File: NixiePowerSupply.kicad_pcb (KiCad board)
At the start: 2 copper layers, 50.8 x 38.1 mm, 17 parts, among them J1 BARREL_JACK, P1 CONN_01X03, P2 CONN_01X02, T1 IRF644, U1 MAX1771

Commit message: More layout
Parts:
- moved C5 3.31 mm to (65.0, 48.8), turned to 0 degrees
- moved R1 2.05 mm to (73.7, 52.8)
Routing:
- net Net-(C1-Pad1): track 25.3 -> 49.5 mm
- net GND: track 14.1 -> 21.4 mm, vias 8 -> 9
- net Net-(R1-Pad1): track 0.00 -> 6.39 mm
- net Net-(R2-Pad2): track 0.00 -> 6.00 mm
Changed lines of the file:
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@@
   (general
     (links 34)
-    (no_connects 33)
+    (no_connects 17)
     (area 40.669999 24.315 97.108334 63.550001)
     (thickness 1.6)
     (drawings 4)
-    (tracks 25)
+    (tracks 47)
     (zones 0)
     (modules 17)
@@
   )
   (setup
-    (last_trace_width 0.508)
+    (last_trace_width 1.016)
     (user_trace_width 0.508)
     (user_trace_width 1.016)
@@
   )
   (module Capacitors_Tantalum_SMD:CP_Tantalum_Case-X_EIA-7343-43_Hand (layer F.Cu)
-    (at 62.23 46.99 270)
+    (at 65.024 48.768)
     (descr "Tantalum capacitor, Case X, EIA 7343-43, 7.3x4.2x4.0mm, Hand soldering footprint")
     (tags "capacitor tantalum smd")
     (attr smd)
-    (fp_text reference C5 (at 0 -3.85 270) (layer F.SilkS)
-      (effects (font (size 1 1) (thickness 0.15)))
-    )
-    (fp_text value 10uF,25V (at 0 3.85 270) (layer F.Fab)
+    (fp_text reference C5 (at 0 -3.85) (layer F.SilkS)
+      (effects (font (size 1 1) (thickness 0.15)))
+    )
+    (fp_text value 10uF,25V (at 0 3.85) (layer F.Fab)
       (effects (font (size 1 1) (thickness 0.15)))
     )
@@
     (fp_line (start -5.95 2.35) (end 3.65 2.35) (layer F.SilkS) (width 0.12))
     (fp_line (start -5.95 -2.35) (end -5.95 2.35) (layer F.SilkS) (width 0.12))
-    (pad 1 smd rect (at -3.775 0 270) (size 3.75 2.7) (layers F.Cu F.Paste F.Mask)
+    (pad 1 smd rect (at -3.775 0) (size 3.75 2.7) (layers F.Cu F.Paste F.Mask)
       (net 9 "Net-(C1-Pad1)"))
-    (pad 2 smd rect (at 3.775 0 270) (size 3.75 2.7) (layers F.Cu F.Paste F.Mask)
+    (pad 2 smd rect (at 3.775 0) (size 3.75 2.7) (layers F.Cu F.Paste F.Mask)
       (net 1 GND))
     (model Capacitors_Tantalum_SMD.3dshapes/CP_Tantalum_Case-X_EIA-7343-43.wrl
@@
   )
   (module Resistors_SMD:R_0805_HandSoldering (layer F.Cu)
-    (at 71.755 52.07 180)
+    (at 73.66 52.832 180)
     (descr "Resistor SMD 0805, hand soldering")
     (tags "resistor 0805")
@@
   (gr_line (start 95.25 25.4) (end 95.25 63.5) (layer Edge.Cuts) (width 0.1))
   (gr_line (start 44.45 25.4) (end 95.25 25.4) (layer Edge.Cuts) (width 0.1))
+  (segment (start 68.799 48.768) (end 68.799 49.321) (width 1.016) (layer F.Cu) (net 1))
+  (segment (start 68.799 49.321) (end 72.31 52.832) (width 1.016) (layer F.Cu) (net 1))
+  (segment (start 66.675 44.41) (end 65.318 44.41) (width 1.016) (layer F.Cu) (net 1))
+  (segment (start 65.318 44.41) (end 65.024 44.704) (width 1.016) (layer F.Cu) (net 1))
+  (via (at 65.024 44.704) (size 0.6) (drill 0.4) (layers F.Cu B.Cu) (net 1))
   (segment (start 91.44 34.036) (end 92.964 34.036) (width 0.508) (layer B.Cu) (net 1))
   (via (at 92.964 34.036) (size 1.016) (drill 0.508) (layers F.Cu B.Cu) (net 1))
@@
   (segment (start 63.580302 30.48) (end 71.755 30.48) (width 3.81) (layer F.Cu) (net 4))
   (segment (start 61.317651 28.217349) (end 63.580302 30.48) (width 3.81) (layer F.Cu) (net 4))
+  (segment (start 75.01 52.832) (end 77.798 52.832) (width 1.016) (layer F.Cu) (net 5))
+  (segment (start 77.798 52.832) (end 77.925 52.705) (width 1.016) (layer F.Cu) (net 5))
+  (segment (start 80.825 53.955) (end 79.175 53.955) (width 1.016) (layer F.Cu) (net 5))
+  (segment (start 79.175 53.955) (end 77.925 52.705) (width 1.016) (layer F.Cu) (net 5))
+  (segment (start 85.725 54.115) (end 83.485 54.115) (width 1.016) (layer F.Cu) (net 6))
+  (segment (start 83.485 54.115) (end 80.825 51.455) (width 1.016) (layer F.Cu) (net 6))
+  (segment (start 66.675 41.91) (end 69.055 41.91) (width 1.016) (layer F.Cu) (net 9))
+  (segment (start 61.249 48.768) (end 61.249 44.679) (width 2.032) (layer F.Cu) (net 9))
+  (segment (start 61.249 44.679) (end 64.018 41.91) (width 2.032) (layer F.Cu) (net 9))
+  (segment (start 64.018 41.91) (end 66.675 41.91) (width 2.032) (layer F.Cu) (net 9))
+  (segment (start 61.249 48.768) (end 60.724 48.768) (width 2.032) (layer F.Cu) (net 9))
+  (segment (start 60.724 48.768) (end 58.442 51.05) (width 2.032) (layer F.Cu) (net 9))
+  (segment (start 58.442 51.05) (end 54.895 51.05) (width 2.032) (layer F.Cu) (net 9))
+  (segment (start 55.682 51.05) (end 54.895 51.05) (width 1.524) (layer F.Cu) (net 9))
+  (segment (start 54.895 53.34) (end 54.895 51.05) (width 3.81) (layer F.Cu) (net 9))
+  (segment (start 54.895 55.88) (end 54.895 53.34) (width 3.81) (layer F.Cu) (net 9))
+  (segment (start 48.93 45.085) (end 48.93 50.245) (width 3.81) (layer F.Cu) (net 9))
+  (segment (start 48.93 50.245) (end 49.735 51.05) (width 3.81) (layer F.Cu) (net 9))
+  (segment (start 49.735 51.05) (end 54.895 51.05) (width 3.81) (layer F.Cu) (net 9))
   (segment (start 54.895 55.88) (end 60.325 55.88) (width 2.032) (layer F.Cu) (net 9))
   (segment (start 48.93 45.085) (end 48.93 40.605) (width 3.81) (layer F.Cu) (net 9))
   (segment (start 48.93 40.605) (end 50.442349 39.092651) (width 3.81) (layer F.Cu) (net 9))
-  (segment (start 54.895 55.88) (end 54.895 51.05) (width 3.81) (layer F.Cu) (net 9))
-  (segment (start 54.895 51.05) (end 48.93 45.085) (width 3.81) (layer F.Cu) (net 9))
   (zone (net 1) (net_name GND) (layer B.Cu) (hatch edge 0.508)
     (connect_pads (clearance 0.508))
@@
     (polygon
       (pts
-        (xy 73.279 35.179) (xy 77.724 35.179) (xy 77.724 38.1) (xy 81.28 38.1) (xy 81.28 42.037)
+        (xy 73.279 35.179) (xy 76.2 35.052) (xy 76.2 37.973) (xy 81.28 38.1) (xy 81.28 42.037)
         (xy 76.327 42.037) (xy 76.327 41.021) (xy 73.279 41.021)
       )
@@
       (pts
         (xy 76.073 28.956) (xy 83.947 28.956) (xy 83.947 34.163) (xy 86.36 36.322) (xy 87.63 36.322)
-        (xy 87.63 47.752) (xy 83.82 47.752) (xy 83.82 38.1) (xy 78.232 33.528) (xy 76.073 33.528)
+        (xy 87.63 47.752) (xy 83.82 47.752) (xy 83.82 39.116) (xy 77.724 33.528) (xy 76.073 33.528)
       )
     )

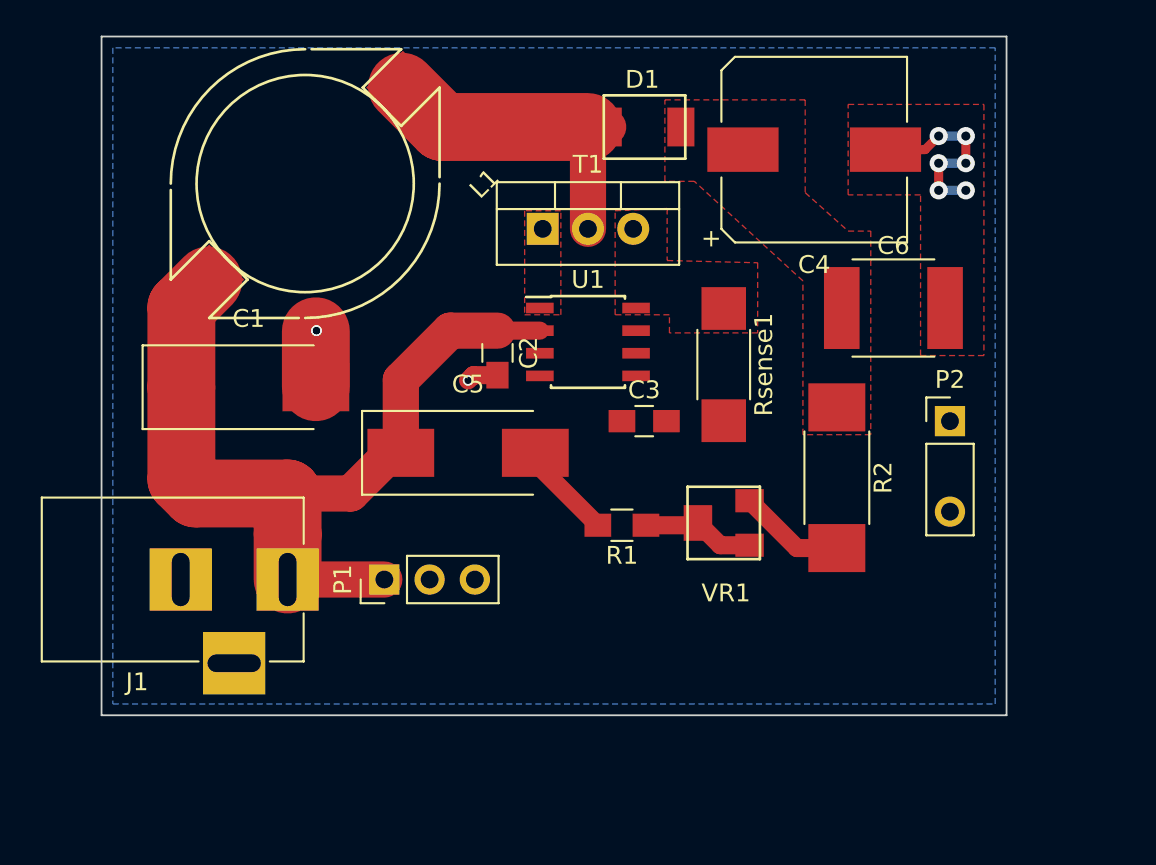
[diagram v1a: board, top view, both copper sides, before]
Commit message: Added mounting holes
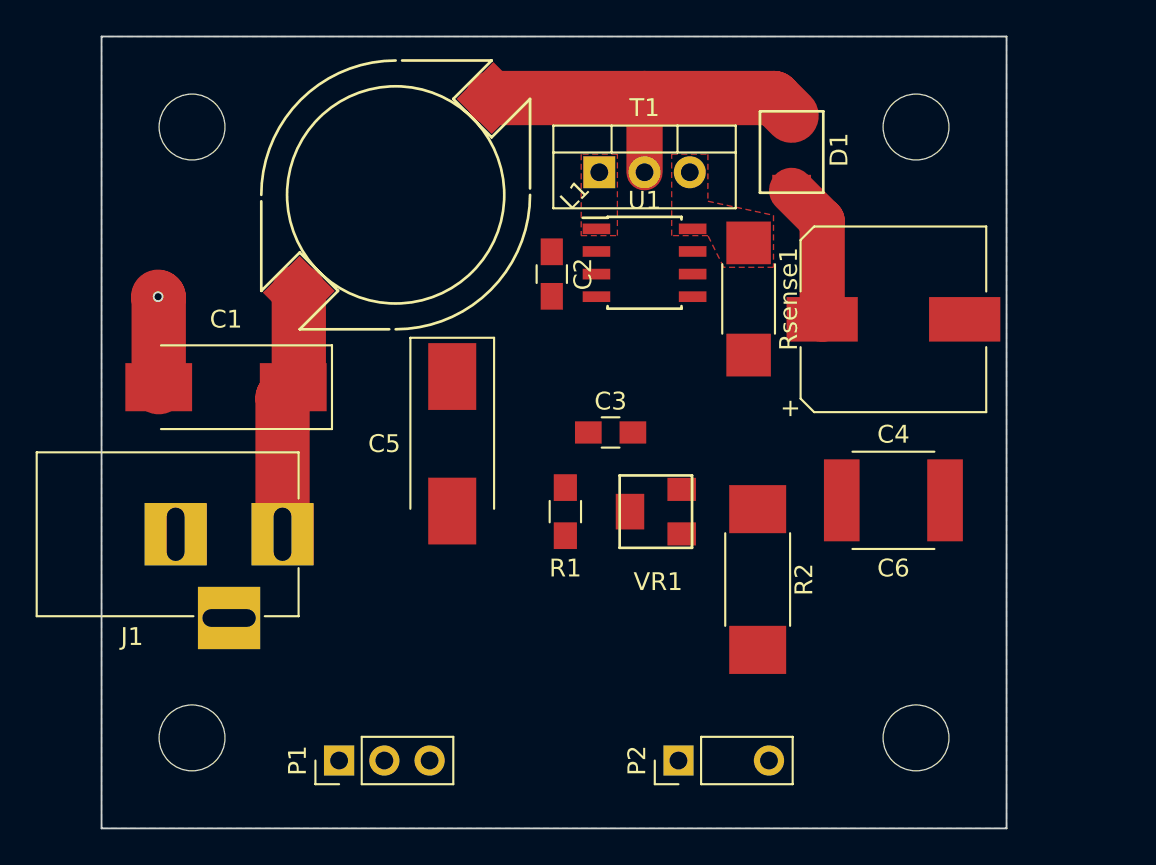
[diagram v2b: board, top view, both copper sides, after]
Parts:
- added REF**: MountingHole_3.7mm, Mounting_Holes:MountingHole_3.7mm, F.Cu at (49.5, 30.5)
- added REF**: MountingHole_3.7mm, Mounting_Holes:MountingHole_3.7mm, F.Cu at (90.2, 30.5)
- added REF**: MountingHole_3.7mm, Mounting_Holes:MountingHole_3.7mm, F.Cu at (90.2, 64.8)
- added REF**: MountingHole_3.7mm, Mounting_Holes:MountingHole_3.7mm, F.Cu at (49.5, 64.8)
- moved P2 24.4 mm to (76.8, 66.0), turned to 90 degrees
- moved C6 10.8 mm to (88.9, 51.4)
- moved C4 10.5 mm to (88.9, 41.3)
- moved P1 10.5 mm to (57.8, 66.0)
- moved D1 8.37 mm to (83.2, 31.9), turned to 90 degrees
- moved R2 7.24 mm to (81.3, 55.9)
- moved U1 5.46 mm to (74.9, 38.1)
- moved C2 5.37 mm to (69.7, 38.7)
- moved L1 5.12 mm to (61.0, 34.3)
- moved T1 4.49 mm to (72.4, 33.0)
- moved Rsense1 3.94 mm to (80.8, 40.1)
- moved VR1 3.86 mm to (75.6, 52.1)
- moved R1 3.27 mm to (70.5, 52.1), turned to 270 degrees
- moved J1 2.56 mm to (54.6, 53.3)
- moved C3 1.99 mm to (73.0, 47.6)
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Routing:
- net Net-(C1-Pad1): track 49.5 -> 14.0 mm
- net GND: track 21.4 -> 5.09 mm, vias 9 -> 1
- net Net-(C4-Pad1): track 0.00 -> 8.06 mm
- net Net-(R1-Pad1): track 6.39 -> 0.00 mm
- net Net-(R2-Pad2): track 6.00 -> 0.00 mm
- net Net-(D1-Pad2): track 17.6 -> 21.4 mm
- removed copper zone on F.Cu, net GND
- removed copper zone on F.Cu, net Net-(C4-Pad1)
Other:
- board size 50.8 x 38.1 mm -> 50.8 x 44.4 mm

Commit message: Embiggened the board
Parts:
- moved REF** 6.35 mm to (96.5, 30.5)
- moved REF** 6.35 mm to (96.5, 64.8)
- moved D1 5.78 mm to (88.9, 31.0)
- moved C6 4.83 mm to (93.7, 51.3)
- moved C4 4.70 mm to (93.6, 41.1)
- moved Rsense1 2.16 mm to (82.9, 40.0)
- moved C5 1.83 mm to (65.2, 49.8)
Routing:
- net Net-(C4-Pad1): track 8.06 -> 0.00 mm
- net GND: track 5.09 -> 12.6 mm, vias 1 -> 7
- net Net-(D1-Pad2): track 21.4 -> 26.7 mm
- added copper zone on F.Cu, net GND
- added copper zone on F.Cu, net Net-(C4-Pad1)
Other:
- board size 50.8 x 44.4 mm -> 57.1 x 44.4 mm
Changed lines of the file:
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@@
   (general
     (links 34)
-    (no_connects 28)
-    (area 40.384999 24.805 99.568572 72.195)
+    (no_connects 22)
+    (area 40.384999 24.805 105.918572 72.195)
     (thickness 1.6)
     (drawings 4)
-    (tracks 14)
+    (tracks 24)
     (zones 0)
     (modules 21)
@@
   )
   (setup
-    (last_trace_width 3.81)
+    (last_trace_width 3.048)
     (user_trace_width 0.508)
     (user_trace_width 1.016)
@@
   )
   (module Mounting_Holes:MountingHole_3.7mm (layer F.Cu)
-    (at 90.17 30.48)
+    (at 96.52 30.48)
     (descr "Mounting Hole 3.7mm, no annular")
     (tags "mounting hole 3.7mm no annular")
@@
   )
   (module Mounting_Holes:MountingHole_3.7mm (layer F.Cu)
-    (at 90.17 64.77)
+    (at 96.52 64.77)
     (descr "Mounting Hole 3.7mm, no annular")
     (tags "mounting hole 3.7mm no annular")
@@
   )
   (module Capacitors_SMD:CP_Elec_10x10 (layer F.Cu)
-    (at 88.9 41.275)
+    (at 93.599 41.148)
     (descr "SMT capacitor, aluminium electrolytic, 10x10")
     (attr smd)
@@
   )
   (module Capacitors_Tantalum_SMD:CP_Tantalum_Case-X_EIA-7343-43_Hand (layer F.Cu)
-    (at 64.135 48.26 270)
+    (at 65.151 49.784 270)
     (descr "Tantalum capacitor, Case X, EIA 7343-43, 7.3x4.2x4.0mm, Hand soldering footprint")
     (tags "capacitor tantalum smd")
@@
   )
   (module nixie:Panasonic_ECWU_Size_B (layer F.Cu)
-    (at 88.9 51.435)
+    (at 93.726 51.308)
     (descr "Capacitor SMD Panasonic ECWU,  B")
     (tags "capacitor Panasonic")
@@
   )
   (module nixie:ES2F (layer F.Cu)
-    (at 83.185 31.885 90)
+    (at 88.9 30.988 90)
     (fp_text reference D1 (at 0.127 2.667 90) (layer F.SilkS)
       (effects (font (size 1 1) (thickness 0.15)))
@@
   )
   (module Resistors_SMD:R_2010_HandSoldering (layer F.Cu)
-    (at 80.772 40.132 270)
+    (at 82.931 40.005 270)
     (descr "Resistor SMD 2010, hand soldering")
     (tags "resistor 2010")
@@
   )
   (gr_line (start 44.45 69.85) (end 44.45 25.4) (layer Edge.Cuts) (width 0.1))
-  (gr_line (start 95.25 69.85) (end 44.45 69.85) (layer Edge.Cuts) (width 0.1))
-  (gr_line (start 95.25 25.4) (end 95.25 69.85) (layer Edge.Cuts) (width 0.1))
-  (gr_line (start 44.45 25.4) (end 95.25 25.4) (layer Edge.Cuts) (width 0.1))
+  (gr_line (start 101.6 69.85) (end 44.45 69.85) (layer Edge.Cuts) (width 0.1))
+  (gr_line (start 101.6 25.4) (end 101.6 69.85) (layer Edge.Cuts) (width 0.1))
+  (gr_line (start 44.45 25.4) (end 101.473 25.4) (layer Edge.Cuts) (width 0.1))
+  (segment (start 83.82 46.482) (end 83.82 45.212) (width 0.508) (layer B.Cu) (net 1))
+  (via (at 83.82 45.212) (size 1.016) (drill 0.508) (layers F.Cu B.Cu) (net 1))
+  (segment (start 82.804 46.482) (end 83.82 46.482) (width 0.508) (layer F.Cu) (net 1))
+  (via (at 83.82 46.482) (size 1.016) (drill 0.508) (layers F.Cu B.Cu) (net 1))
+  (segment (start 81.788 46.482) (end 82.804 46.482) (width 0.508) (layer B.Cu) (net 1))
+  (via (at 82.804 46.482) (size 1.016) (drill 0.508) (layers F.Cu B.Cu) (net 1))
+  (segment (start 81.788 45.212) (end 81.788 46.482) (width 0.508) (layer F.Cu) (net 1))
+  (via (at 81.788 46.482) (size 1.016) (drill 0.508) (layers F.Cu B.Cu) (net 1))
+  (segment (start 82.804 45.212) (end 81.788 45.212) (width 0.508) (layer B.Cu) (net 1))
+  (via (at 81.788 45.212) (size 1.016) (drill 0.508) (layers F.Cu B.Cu) (net 1))
+  (segment (start 82.804 43.282) (end 82.804 45.212) (width 0.508) (layer F.Cu) (net 1))
+  (via (at 82.804 45.212) (size 1.016) (drill 0.508) (layers F.Cu B.Cu) (net 1))
   (segment (start 47.66 45.085) (end 47.66 40.04) (width 3.048) (layer F.Cu) (net 1))
   (segment (start 47.66 40.04) (end 47.625 40.005) (width 3.048) (layer F.Cu) (net 1))
   (via (at 47.625 40.005) (size 0.6) (drill 0.4) (layers F.Cu B.Cu) (net 1))
-  (segment (start 83.185 34.036) (end 84.9 35.751) (width 2.54) (layer F.Cu) (net 3))
-  (segment (start 84.9 35.751) (end 84.9 41.275) (width 2.54) (layer F.Cu) (net 3))
-  (segment (start 83.185 33.925) (end 83.185 34.036) (width 2.032) (layer F.Cu) (net 3))
+  (segment (start 74.93 28.852349) (end 75.025651 28.948) (width 3.048) (layer F.Cu) (net 4))
+  (segment (start 75.025651 28.948) (end 88.9 28.948) (width 3.048) (layer F.Cu) (net 4))
   (segment (start 66.397651 28.852349) (end 74.93 28.852349) (width 3.048) (layer F.Cu) (net 4))
-  (segment (start 74.93 28.852349) (end 82.192349 28.852349) (width 3.048) (layer F.Cu) (net 4))
   (segment (start 74.93 33.02) (end 74.93 28.852349) (width 2.032) (layer F.Cu) (net 4))
-  (segment (start 82.192349 28.852349) (end 83.185 29.845) (width 3.048) (layer F.Cu) (net 4))
   (segment (start 55.522349 39.727651) (end 55.522349 44.772651) (width 3.048) (layer F.Cu) (net 9))
+  (segment (start 55.21 48.803) (end 54.61 49.403) (width 3.048) (layer F.Cu) (net 9))
+  (segment (start 54.61 49.403) (end 54.61 53.34) (width 3.048) (layer F.Cu) (net 9))
+  (segment (start 55.21 45.085) (end 55.21 48.803) (width 3.048) (layer F.Cu) (net 9))
   (segment (start 55.522349 44.772651) (end 55.21 45.085) (width 3.048) (layer F.Cu) (net 9))
-  (segment (start 54.61 53.34) (end 54.61 45.685) (width 3.048) (layer F.Cu) (net 9))
-  (segment (start 54.61 45.685) (end 55.21 45.085) (width 3.048) (layer F.Cu) (net 9))
   (zone (net 1) (net_name GND) (layer B.Cu) (hatch edge 0.508)
     (connect_pads (clearance 0.254))
@@
     (polygon
       (pts
-        (xy 95.25 25.4) (xy 44.45 25.4) (xy 44.45 69.85) (xy 95.25 69.85)
+        (xy 101.6 25.4) (xy 44.45 25.4) (xy 44.45 69.85) (xy 101.6 69.85)
       )
     )
@@
       )
     )
+  )
+  (zone (net 1) (net_name GND) (layer F.Cu) (hatch edge 0.508)
+    (priority 1)
+    (connect_pads yes (clearance 0.254))
+    (min_thickness 0.254)
+    (fill yes (arc_segments 16) (thermal_gap 0.508) (thermal_bridge_width 0.508) (smoothing chamfer) (radius 0.254))
+    (polygon
+      (pts
+        (xy 81.026 41.91) (xy 84.582 41.91) (xy 84.582 47.244) (xy 81.026 47.244)
+      )
+    )
+  )
+  (zone (net 3) (net_name "Net-(C4-Pad1)") (layer F.Cu) (hatch edge 0.508)
+    (priority 1)
+    (connect_pads yes (clearance 0.254))
+    (min_thickness 0.254)
+    (fill yes (arc_segments 16) (thermal_gap 0.508) (thermal_bridge_width 0.508) (smoothing chamfer) (radius 0.254))
+    (polygon
+      (pts
+        (xy 87.63 53.848) (xy 92.202 53.848) (xy 92.202 31.75) (xy 87.63 31.75)
+      )
+    )
+  )
+  (zone (net 1) (net_name GND) (layer F.Cu) (hatch edge 0.508)
+    (priority 1)
+    (connect_pads yes (clearance 0.254))
+    (min_thickness 0.254)
+    (fill yes (arc_segments 16) (thermal_gap 0.508) (thermal_bridge_width 0.508) (smoothing chamfer) (radius 0.254))
+    (polygon
+      (pts
+        (xy 95.25 35.56) (xy 95.25 57.15) (xy 100.33 57.15) (xy 100.33 35.56)
+      )
+    )

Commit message: More layout
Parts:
- removed C1: 100uF, 35V, Capacitors_Tantalum_SMD:CP_Tantalum_Case-X_EIA-7343-43_Hand
- moved D1 13.5 mm to (76.5, 36.2), turned to 180 degrees
- moved T1 9.12 mm to (69.8, 41.8)
- moved U1 9.12 mm to (72.4, 46.9)
- moved C2 9.12 mm to (67.2, 47.5)
- moved R1 6.48 mm to (67.7, 57.9)
- moved VR1 6.48 mm to (72.8, 57.9)
- moved REF** 6.35 mm to (90.2, 64.8)
- moved REF** 6.35 mm to (90.2, 30.5)
- moved Rsense1 5.82 mm to (79.9, 45.0)
- moved P2 5.72 mm to (82.5, 66.0), turned to 270 degrees
- moved C4 5.08 mm to (88.5, 41.0)
- moved C3 4.89 mm to (75.1, 52.1), turned to 270 degrees
- moved C6 4.45 mm to (89.3, 51.2)
- moved L1 4.32 mm to (58.9, 38.1)
- moved C5 3.32 mm to (62.7, 52.1)
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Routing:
- net Net-(C4-Pad1): track 0.00 -> 37.4 mm
- net Net-(C1-Pad1): track 14.0 -> 41.4 mm
- net GND: track 12.6 -> 38.7 mm, vias 7 -> 22
- net Net-(P1-Pad2): track 0.00 -> 22.3 mm
- net Net-(R2-Pad2): track 0.00 -> 16.5 mm
- net Net-(D1-Pad2): track 26.7 -> 17.1 mm
- net Net-(R1-Pad1): track 0.00 -> 7.61 mm
- net Net-(Rsense1-Pad1): track 0.00 -> 4.76 mm
- net Net-(C3-Pad1): track 0.00 -> 2.07 mm
- removed copper zone on F.Cu, net Net-(C4-Pad1)
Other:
- board size 57.1 x 44.4 mm -> 50.8 x 44.4 mm
